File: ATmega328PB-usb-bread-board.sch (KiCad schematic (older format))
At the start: 28 parts, among them J1 Conn_01x17, J2 Conn_01x17, J3 USB_B_Micro, J4 AVR-ISP-6, J5 Grove-I2C-connector, J6 Grove-I2C-connector, J7 Grove-I2C-connector, U1 ATmega328PB-MU, U2 CP2102N-A01-GQFN28, U3 LMV358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

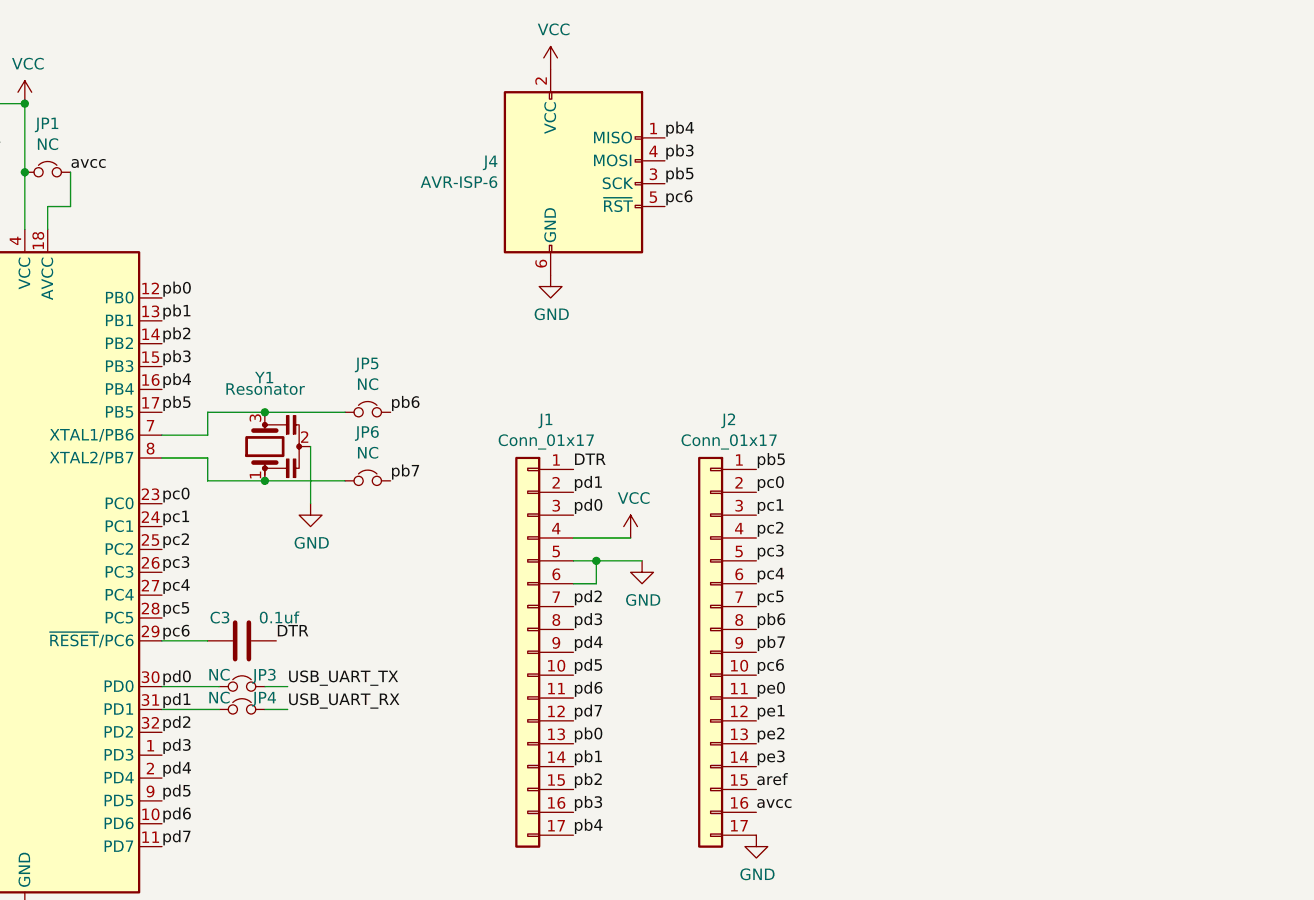
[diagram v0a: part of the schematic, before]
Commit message: Put 3V3 regulator and 16MHz MEMS to shematic
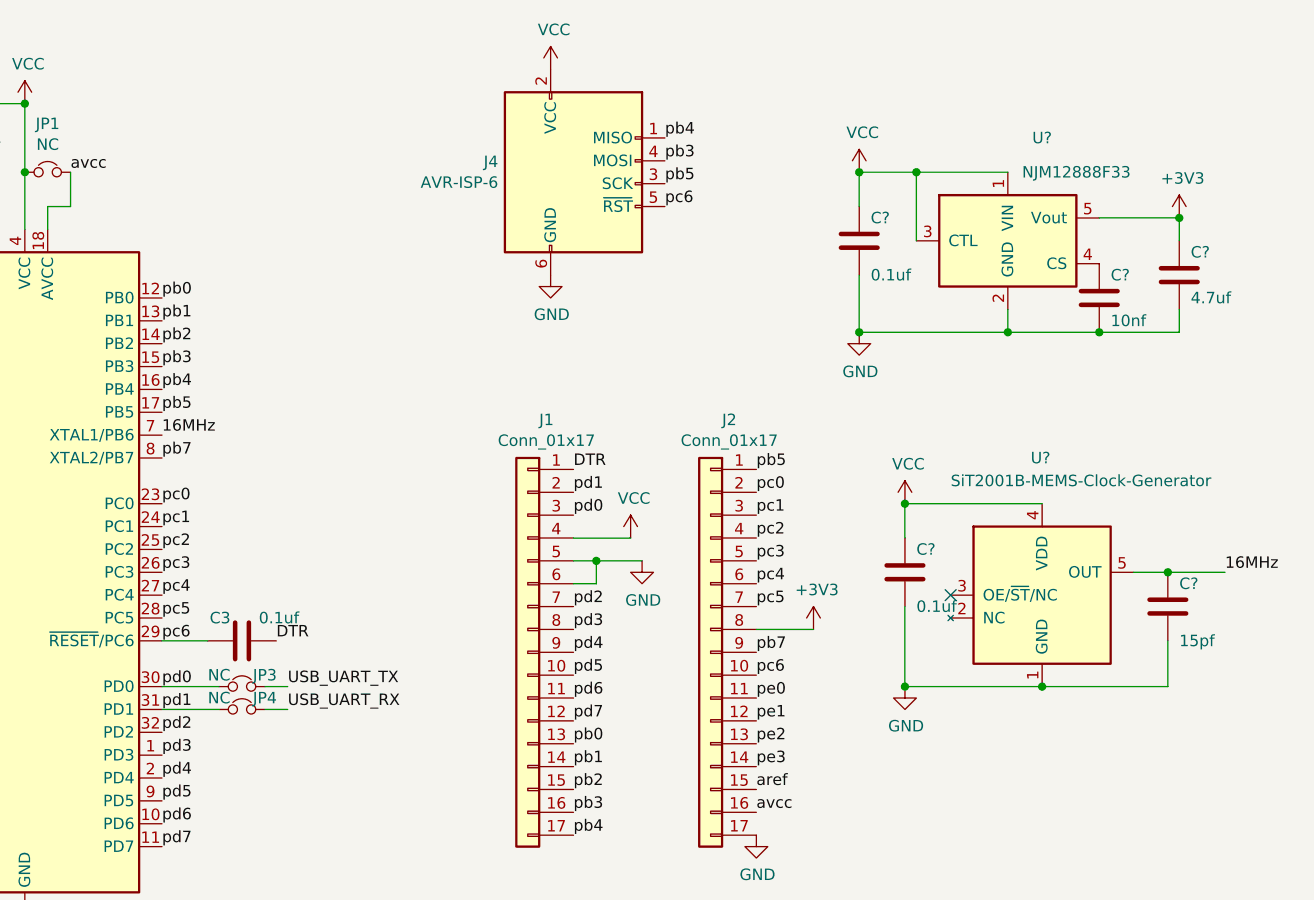
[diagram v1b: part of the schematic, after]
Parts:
- removed JP5, JP6: NC, Jumper:SolderJumper-2_P1.3mm_Bridged_RoundedPad1.0x1.5mm, symbol ATmega328PB-usb-bread-board-rescue:Jumper_NC_Small-Device
- removed Y1: Resonator, Crystal:Resonator_SMD_Murata_CSTxExxV-3Pin_3.0x1.1mm, symbol Device:Resonator
- added C? (x2): 0.1uf, Capacitor_SMD:C_0603_1608Metric, symbol Device:C
- added C?: 10nf, Capacitor_SMD:C_0603_1608Metric, symbol Device:C
- added C?: 4.7uf, Capacitor_SMD:C_0402_1005Metric, symbol Device:C
- added C?: 15pf, Capacitor_SMD:C_0603_1608Metric, symbol Device:C
- added U?: NJM12888F33, Package_TO_SOT_SMD:SOT-23-5, symbol my-kicad-symbols:NJM12888F33
- added U?: SiT2001B-MEMS-Clock-Generator, symbol my-kicad-symbols:SiT2001B-MEMS-Clock-Generator
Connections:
- net GND: now also C?.2, C?.2, C?.2, C?.2, C?.2, U?.1 (GND), U?.2 (GND)
- net VCC: now also C?.1, C?.1, U?.1 (VIN), U?.3 (CTL), U?.4 (VDD)
- net pb7: now also U1.8 (XTAL2/PB7)
- net 16MHz: now reaches U1.7 (XTAL1/PB6)
- net 16MHz: now also C?.1, U?.5 (OUT)
- net pb6 renamed +3V3
- net +3V3: now also C?.1, U?.5 (Vout)
- new net: C?.1, U?.4 (CS)
- no-connect marks 23 -> 24
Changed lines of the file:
@@
 Text Label 6150 2550 0    50   ~ 0
 pb5
-Text Label 7150 2550 0    50   ~ 0
-pb6
-Text Label 7150 2850 0    50   ~ 0
+Text Label 6150 2750 0    50   ~ 0
 pb7
 Text Label 6150 2950 0    50   ~ 0
@@
 Text Label 8750 3600 0    50   ~ 0
 pb7
-Text Label 8750 3500 0    50   ~ 0
-pb6
 Wire Wire Line
 	8250 3200 8050 3200
@@
 NoConn ~ 3450 3250
 NoConn ~ 3450 3150
-$Comp
-L Device:Resonator Y1
-U 1 1 5F78A738
-P 6600 2700
-F 0 "Y1" V 6900 2700 50  0000 C CNN
-F 1 "Resonator" V 6850 2700 50  0000 C CNN
-F 2 "Crystal:Resonator_SMD_Murata_CSTxExxV-3Pin_3.0x1.1mm" H 6575 2700 50  0001 C CNN
-F 3 "~" H 6575 2700 50  0001 C CNN
-	1    6600 2700
-	0    -1   -1   0
-$EndComp
-$Comp
-L power:GND #PWR0111
-U 1 1 5F796F09
-P 6800 2950
-F 0 "#PWR0111" H 6800 2700 50  0001 C CNN
-F 1 "GND" H 6805 2777 50  0000 C CNN
-F 2 "" H 6800 2950 50  0001 C CNN
-F 3 "" H 6800 2950 50  0001 C CNN
-	1    6800 2950
-	1    0    0    -1
-$EndComp
 $Comp
 L Connector:AVR-ISP-6 J4
@@
 Wire Wire Line
 	2950 1400 2850 1400
-Wire Wire Line
-	6800 2950 6800 2700
-$Comp
-L ATmega328PB-usb-bread-board-rescue:Jumper_NC_Small-Device JP5
-U 1 1 5F8E4AE0
-P 7050 2550
-F 0 "JP5" H 7050 2762 50  0000 C CNN
-F 1 "NC" H 7050 2671 50  0000 C CNN
-F 2 "Jumper:SolderJumper-2_P1.3mm_Bridged_RoundedPad1.0x1.5mm" H 7050 2550 50  0001 C CNN
-F 3 "~" H 7050 2550 50  0001 C CNN
-	1    7050 2550
-	1    0    0    -1
-$EndComp
-$Comp
-L ATmega328PB-usb-bread-board-rescue:Jumper_NC_Small-Device JP6
-U 1 1 5F8E582D
-P 7050 2850
-F 0 "JP6" H 7050 3062 50  0000 C CNN
-F 1 "NC" H 7050 2971 50  0000 C CNN
-F 2 "Jumper:SolderJumper-2_P1.3mm_Bridged_RoundedPad1.0x1.5mm" H 7050 2850 50  0001 C CNN
-F 3 "~" H 7050 2850 50  0001 C CNN
-	1    7050 2850
-	1    0    0    -1
-$EndComp
-Wire Wire Line
-	6950 2850 6600 2850
-Wire Wire Line
-	6350 2850 6350 2750
-Wire Wire Line
-	6350 2750 6150 2750
-Connection ~ 6600 2850
-Wire Wire Line
-	6600 2850 6350 2850
-Wire Wire Line
-	6150 2650 6350 2650
-Wire Wire Line
-	6350 2650 6350 2550
-Wire Wire Line
-	6350 2550 6600 2550
-Connection ~ 6600 2550
-Wire Wire Line
-	6600 2550 6950 2550
+$Comp
+L my-kicad-symbols:NJM12888F33 U?
+U 1 1 5F8C64C1
+P 9850 1800
+F 0 "U?" H 10000 2250 50  0000 C CNN
+F 1 "NJM12888F33" H 10150 2100 50  0000 C CNN
+F 2 "Package_TO_SOT_SMD:SOT-23-5" H 9850 1800 50  0001 C CNN
+F 3 "" H 9850 1800 50  0001 C CNN
+	1    9850 1800
+	1    0    0    -1
+$EndComp
+$Comp
+L power:VCC #PWR?
+U 1 1 5F8C761A
+P 9200 1500
+F 0 "#PWR?" H 9200 1350 50  0001 C CNN
+F 1 "VCC" H 9215 1673 50  0000 C CNN
+F 2 "" H 9200 1500 50  0001 C CNN
+F 3 "" H 9200 1500 50  0001 C CNN
+	1    9200 1500
+	1    0    0    -1
+$EndComp
+$Comp
+L power:GND #PWR?
+U 1 1 5F8C7AD0
+P 9200 2200
+F 0 "#PWR?" H 9200 1950 50  0001 C CNN
+F 1 "GND" H 9205 2027 50  0000 C CNN
+F 2 "" H 9200 2200 50  0001 C CNN
+F 3 "" H 9200 2200 50  0001 C CNN
+	1    9200 2200
+	1    0    0    -1
+$EndComp
+$Comp
+L Device:C C?
+U 1 1 5F8C87B4
+P 9200 1800
+F 0 "C?" H 9250 1900 50  0000 L CNN
+F 1 "0.1uf" H 9250 1650 50  0000 L CNN
+F 2 "Capacitor_SMD:C_0603_1608Metric" H 9238 1650 50  0001 C CNN
+F 3 "~" H 9200 1800 50  0001 C CNN
+	1    9200 1800
+	1    0    0    -1
+$EndComp
+Wire Wire Line
+	9200 1500 9450 1500
+Wire Wire Line
+	9450 1500 9450 1800
+Connection ~ 9450 1500
+Wire Wire Line
+	9450 1500 9850 1500
+Wire Wire Line
+	9200 1650 9200 1500
+Connection ~ 9200 1500
+$Comp
+L Device:C C?
+U 1 1 5F8D0B51
+P 10250 2050
+F 0 "C?" H 10300 2150 50  0000 L CNN
+F 1 "10nf" H 10300 1950 50  0000 L CNN
+F 2 "Capacitor_SMD:C_0603_1608Metric" H 10288 1900 50  0001 C CNN
+F 3 "~" H 10250 2050 50  0001 C CNN
+	1    10250 2050
+	1    0    0    -1
+$EndComp
+Wire Wire Line
+	9200 1950 9200 2200
+Wire Wire Line
+	9200 2200 9850 2200
+Connection ~ 9200 2200
+Wire Wire Line
+	9850 2200 9850 2100
+Connection ~ 9850 2200
+Wire Wire Line
+	9850 2200 10250 2200
+$Comp
+L Device:C C?
+U 1 1 5F8D5F68
+P 10600 1950
+F 0 "C?" H 10650 2050 50  0000 L CNN
+F 1 "4.7uf" H 10650 1850 50  0000 L CNN
+F 2 "Capacitor_SMD:C_0402_1005Metric" H 10638 1800 50  0001 C CNN
+F 3 "~" H 10600 1950 50  0001 C CNN
+	1    10600 1950
+	1    0    0    -1
+$EndComp
+$Comp
+L power:+3V3 #PWR?
+U 1 1 5F8D6BD8
+P 10600 1700
+F 0 "#PWR?" H 10600 1550 50  0001 C CNN
+F 1 "+3V3" H 10615 1873 50  0000 C CNN
+F 2 "" H 10600 1700 50  0001 C CNN
+F 3 "" H 10600 1700 50  0001 C CNN
+	1    10600 1700
+	1    0    0    -1
+$EndComp
+Wire Wire Line
+	10600 1700 10600 1800
+Wire Wire Line
+	10600 1700 10250 1700
+Connection ~ 10600 1700
+Wire Wire Line
+	10250 2200 10600 2200
+Wire Wire Line
+	10600 2200 10600 2100
+Connection ~ 10250 2200
+$Comp
+L power:+3V3 #PWR?
+U 1 1 5F8DE3AD
+P 9000 3500
+F 0 "#PWR?" H 9000 3350 50  0001 C CNN
+F 1 "+3V3" H 9015 3673 50  0000 C CNN
+F 2 "" H 9000 3500 50  0001 C CNN
+F 3 "" H 9000 3500 50  0001 C CNN
+	1    9000 3500
+	1    0    0    -1
+$EndComp
+Wire Wire Line
+	9000 3500 8750 3500
+$Comp
+L my-kicad-symbols:SiT2001B-MEMS-Clock-Generator U?
+U 1 1 5F8E3D90
+P 10000 3350
+F 0 "U?" H 9950 3950 50  0000 L CNN
+F 1 "SiT2001B-MEMS-Clock-Generator" H 9600 3850 50  0000 L CNN
+F 2 "" H 10000 3350 50  0001 C CNN
+F 3 "" H 10000 3350 50  0001 C CNN
+	1    10000 3350
+	1    0    0    -1
+$EndComp
+$Comp
+L power:VCC #PWR?
+U 1 1 5F8E86D4
+P 9400 2950
+F 0 "#PWR?" H 9400 2800 50  0001 C CNN
+F 1 "VCC" H 9415 3123 50  0000 C CNN
+F 2 "" H 9400 2950 50  0001 C CNN
+F 3 "" H 9400 2950 50  0001 C CNN
+	1    9400 2950
+	1    0    0    -1
+$EndComp
+$Comp
+L power:GND #PWR?
+U 1 1 5F8E86DA
+P 9400 3750
+F 0 "#PWR?" H 9400 3500 50  0001 C CNN
+F 1 "GND" H 9405 3577 50  0000 C CNN
+F 2 "" H 9400 3750 50  0001 C CNN
+F 3 "" H 9400 3750 50  0001 C CNN
+	1    9400 3750
+	1    0    0    -1
+$EndComp
+$Comp
+L Device:C C?
+U 1 1 5F8E86E0
+P 9400 3250
+F 0 "C?" H 9450 3350 50  0000 L CNN
+F 1 "0.1uf" H 9450 3100 50  0000 L CNN
+F 2 "Capacitor_SMD:C_0603_1608Metric" H 9438 3100 50  0001 C CNN
+F 3 "~" H 9400 3250 50  0001 C CNN
+	1    9400 3250
+	1    0    0    -1
+$EndComp
+Wire Wire Line
+	9400 3100 9400 2950
+Connection ~ 9400 2950
+Wire Wire Line
+	10000 3750 9400 3750
+Wire Wire Line
+	9400 3400 9400 3750
+Connection ~ 9400 3750
+Wire Wire Line
+	9400 2950 10000 2950
+$Comp
+L Device:C C?
+U 1 1 5F8F13DA
+P 10550 3400
+F 0 "C?" H 10600 3500 50  0000 L CNN
+F 1 "15pf" H 10600 3250 50  0000 L CNN
+F 2 "Capacitor_SMD:C_0603_1608Metric" H 10588 3250 50  0001 C CNN
+F 3 "~" H 10550 3400 50  0001 C CNN
+	1    10550 3400
+	1    0    0    -1
+$EndComp
+Wire Wire Line
+	10550 3550 10550 3750
+Wire Wire Line
+	10550 3750 10000 3750
+Connection ~ 10000 3750
+Text Label 10800 3250 0    50   ~ 0
+16MHz
+Wire Wire Line
+	10800 3250 10550 3250
+Connection ~ 10550 3250
+Wire Wire Line
+	10550 3250 10400 3250
+Text Label 6150 2650 0    50   ~ 0
+16MHz
+NoConn ~ 9600 3350
 $EndSCHEMATC
